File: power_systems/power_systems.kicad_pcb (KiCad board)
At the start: 2 copper layers, 75.7 x 39.9 mm, 13 parts, among them J1 Screw_Terminal_01x02, J2 Screw_Terminal_01x02, J3 Screw_Terminal_01x02, U1 LM2576HVS-5, U2 LM2576HVS-12

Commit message: power systems update and fc redesign
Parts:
- removed C1, C4: 100 uF, Capacitor_SMD:CP_Elec_4x3
- removed C2: 1000 uF, Capacitor_SMD:CP_Elec_4x3
- removed C3: C, Capacitor_SMD:CP_Elec_4x3
- removed D1: D_Schottky, Diode_SMD:D_0201_0603Metric
- removed J1, J2, J3: Screw_Terminal_01x02, TerminalBlock:TerminalBlock_MaiXu_MX126-5.0-02P_1x02_P5.00mm
- removed L2: L, Inductor_SMD:L_7.3x7.3_H3.5
- removed U2: LM2576HVS-12, Package_TO_SOT_SMD:TO-263-5_TabPin3
- added Q1: BSC520N15NS3GATMA1, avi_lib:TRANS_BSC520N15NS3GATMA1, F.Cu at (140.5, 69.3)
- added Q2: BSC520N15NS3GATMA1, avi_lib:TRANS_BSC520N15NS3GATMA1, F.Cu at (117.9, 84.7)
- added Q3: BSC520N15NS3GATMA1, avi_lib:TRANS_BSC520N15NS3GATMA1, F.Cu at (117.9, 91.4)
- D2: value D_Schottky -> PNE20010ER-Q; footprint Diode_SMD:D_0201_0603Metric -> avi_lib:CR_CFP3_SOD123W_NEX
- L1: value 100 uH -> 33uH; footprint Inductor_SMD:L_7.3x7.3_H3.5 -> avi_lib:7443633300
- U1: value LM2576HVS-5 -> LTC7801EFE-PBF; footprint Package_TO_SOT_SMD:TO-263-5_TabPin3 -> avi_lib:FE_24_ADI
- moved U1 86.4 mm to (140.3, 58.5)
- moved L1 58.6 mm to (123.9, 62.1)
- moved D2 42.7 mm to (105.7, 52.0)
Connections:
- D2 pad 2: GND -> /battery_step_down/DRVCC
- L1 pad 1: Net-(D1-K) -> /battery_step_down/SW
- L1 pad 2: Net-(J2-Pin_1) -> /battery_step_down/SENSE+
- U1 pad 1: Net-(J1-Pin_2) -> /battery_step_down/SENSE-
- U1 pad 2: Net-(D1-K) -> Net-(U1-SS)
- U1 pad 3: GND -> Net-(U1-VFB)
- U1 pad 4: Net-(J2-Pin_1) -> Net-(U1-ITH)
- U1 pad 5: GND -> Net-(U1-CRUMPEN)
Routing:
- net Net-(J3-Pin_1): track 56.9 -> 0.00 mm
- net Net-(J1-Pin_2): track 55.2 -> 0.00 mm
- net Net-(J2-Pin_1): track 55.0 -> 0.00 mm
- net Net-(D1-K): track 49.4 -> 0.00 mm
- net Net-(D2-K): track 45.5 -> 0.00 mm
- net GND: vias 3 -> 0
- removed copper zone on B.Cu, net GND
- removed copper zone on F.Cu, net GND
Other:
- board outline removed
- board text removed: "+12V"
- board text removed: "+5V"
- board text removed: "+V"
- board text removed: "GND"

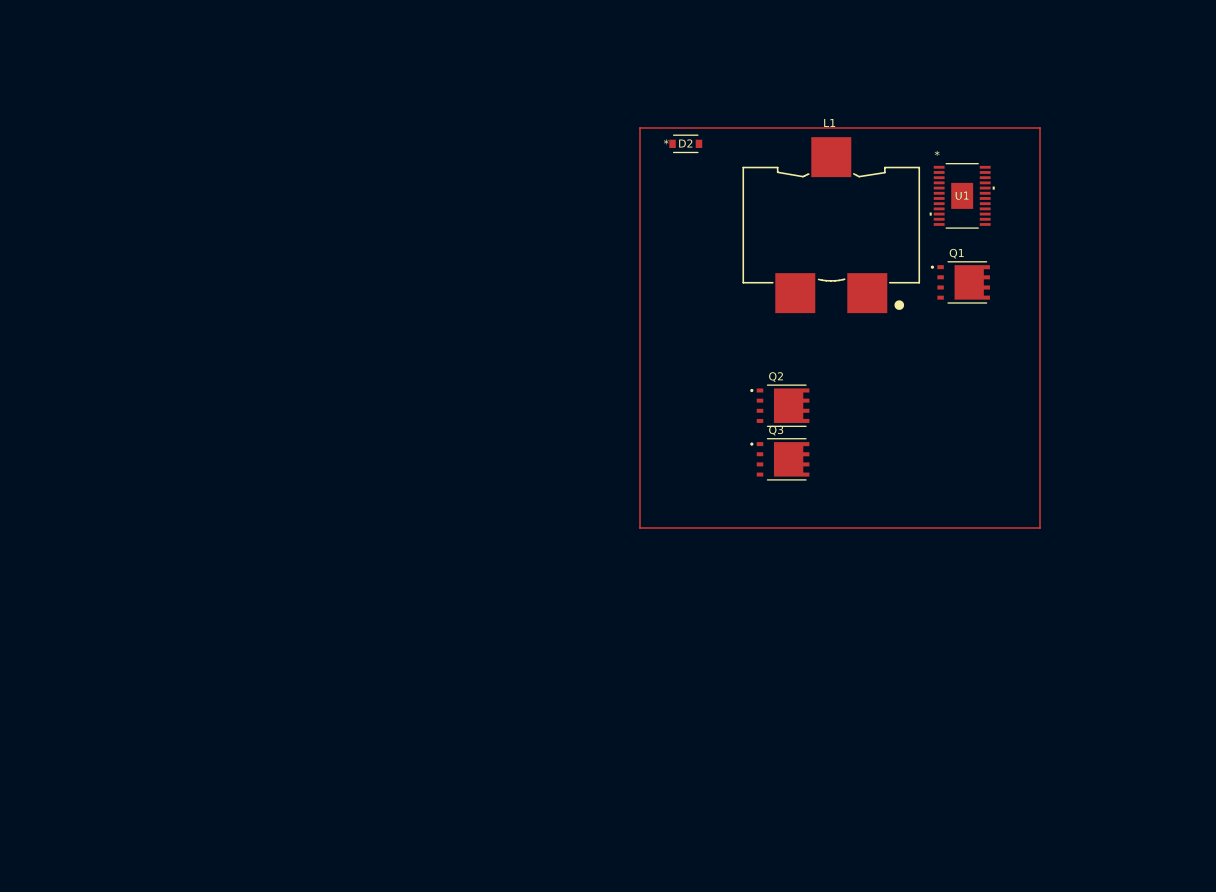
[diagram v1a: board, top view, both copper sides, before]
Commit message: Schematics and layouting for power systems board
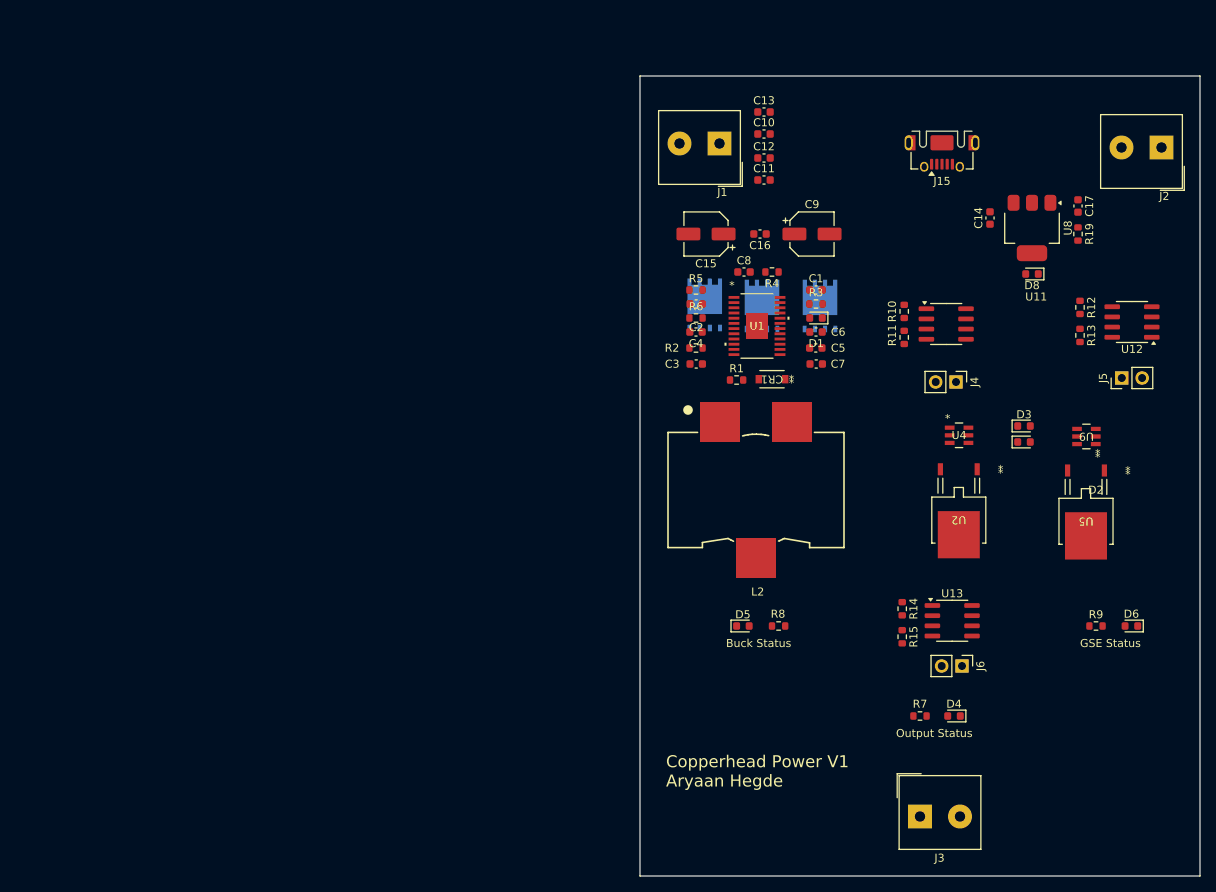
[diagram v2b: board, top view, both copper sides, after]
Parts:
- removed L1: 33uH, avi_lib:7443633300
- removed Q1, Q2: BSC520N15NS3GATMA1, avi_lib:TRANS_BSC520N15NS3GATMA1
- added C1: 0.1uF, Capacitor_SMD:C_0603_1608Metric, F.Cu at (122.0, 70.2)
- added C10: 0.47uF, Capacitor_SMD:C_0603_1608Metric, F.Cu at (115.5, 50.8)
- added C11: 0.47uF, Capacitor_SMD:C_0603_1608Metric, F.Cu at (115.5, 56.5)
- added C12: 0.47uF, Capacitor_SMD:C_0603_1608Metric, F.Cu at (115.5, 53.8)
- added C13: 0.47uF, Capacitor_SMD:C_0603_1608Metric, F.Cu at (115.5, 48.0)
- added C14: 22uF, Capacitor_SMD:C_0603_1608Metric, F.Cu at (143.8, 61.2)
- added C15: 68uF, Capacitor_SMD:CP_Elec_5x3, F.Cu at (108.2, 63.2)
- added C16: 10uF, Capacitor_SMD:C_0603_1608Metric, F.Cu at (115.0, 63.2)
- added C17: 22uF, Capacitor_SMD:C_0603_1608Metric, F.Cu at (154.8, 59.8)
- added C2: 0.1uF, Capacitor_SMD:C_0603_1608Metric, F.Cu at (107.0, 72.0)
- added C3: 100pF, Capacitor_SMD:C_0603_1608Metric, F.Cu at (107.0, 79.5)
- added C4: 3.3nF, Capacitor_SMD:C_0603_1608Metric, F.Cu at (107.0, 75.5)
- added C5: 4.7uF, Capacitor_SMD:C_0603_1608Metric, F.Cu at (122.0, 77.5)
- added C6: 1uF, Capacitor_SMD:C_0603_1608Metric, F.Cu at (122.0, 75.5)
- added C7: 0.1uF, Capacitor_SMD:C_0603_1608Metric, F.Cu at (122.0, 79.5)
- added C8: 0.1uF, Capacitor_SMD:C_0603_1608Metric, F.Cu at (113.0, 68.0)
- added C9: 100uF, Capacitor_SMD:CP_Elec_5x3, F.Cu at (121.5, 63.2)
- added CR1: PNE20010ER-QX, footprints:CR_CFP3_SOD123W_NEX, F.Cu at (116.5, 81.4)
- added D1: DS18015, Diode_SMD:D_0603_1608Metric, F.Cu at (122.0, 73.8)
- added D3: D_Schottky, Diode_SMD:D_0603_1608Metric, F.Cu at (148.0, 87.2)
- added D4: LED_VOUT, Diode_SMD:D_0603_1608Metric, F.Cu at (139.2, 123.5)
- added D5: LED_24, Diode_SMD:D_0603_1608Metric, F.Cu at (112.9, 112.2)
- added D6: LED_GSE, Diode_SMD:D_0603_1608Metric, F.Cu at (161.4, 112.2)
- added D8: LED_STM, Diode_SMD:D_0603_1608Metric, F.Cu at (149.0, 68.2)
- added J1: Screw_Terminal_01x02, TerminalBlock_Altech:Altech_AK100_1x02_P5.00mm, F.Cu at (109.9, 51.9)
- added J15: USB_B_Micro, Connector_USB:USB_Micro-AB_Molex_47590-0001, F.Cu at (137.8, 51.5)
- added J2: Screw_Terminal_01x02, TerminalBlock_Altech:Altech_AK100_1x02_P5.00mm, F.Cu at (165.2, 52.4)
- added J3: Screw_Terminal_01x02, TerminalBlock_Altech:Altech_AK100_1x02_P5.00mm, F.Cu at (135.0, 136.1)
- added J4: Conn_01x02_Pin, Connector_PinHeader_2.54mm:PinHeader_1x02_P2.54mm_Vertical, F.Cu at (139.5, 81.8)
- added J5: Conn_01x02_Pin, Connector_PinHeader_2.54mm:PinHeader_1x02_P2.54mm_Vertical, F.Cu at (160.2, 81.2)
- added J6: Conn_01x02_Pin, Connector_PinHeader_2.54mm:PinHeader_1x02_P2.54mm_Vertical, F.Cu at (140.2, 117.2)
- added L2: WE-HCF_2013, footprints:WE-HCF_2013, F.Cu at (114.5, 95.2)
- added Q4: BSC520N15NS3GATMA1, footprints:TRANS_BSC520N15NS3GATMA1, B.Cu at (122.5, 72.2)
- added Q5: BSC520N15NS3GATMA1, footprints:TRANS_BSC520N15NS3GATMA1, B.Cu at (115.2, 72.2)
- added R1: 36.5k, Resistor_SMD:R_0603_1608Metric, F.Cu at (112.1, 81.5)
- added R10: 320k, Resistor_SMD:R_0603_1608Metric, F.Cu at (133.0, 72.9)
- added R11: 40k, Resistor_SMD:R_0603_1608Metric, F.Cu at (133.0, 76.2)
- added R12: 320k, Resistor_SMD:R_0603_1608Metric, F.Cu at (155.0, 72.4)
- added R13: 40k, Resistor_SMD:R_0603_1608Metric, F.Cu at (155.0, 75.9)
- added R14: 320k, Resistor_SMD:R_0603_1608Metric, F.Cu at (132.8, 110.1)
- added R15: 40k, Resistor_SMD:R_0603_1608Metric, F.Cu at (132.8, 113.6)
- added R19: 1k5, Resistor_SMD:R_0603_1608Metric, F.Cu at (154.8, 63.2)
- added R2: R_US, Resistor_SMD:R_0603_1608Metric, F.Cu at (107.0, 77.5)
- added R3: 10, Resistor_SMD:R_0603_1608Metric, F.Cu at (122.0, 72.0)
- added R4: 6m, Resistor_SMD:R_0603_1608Metric, F.Cu at (116.5, 68.0)
- added R5: 806k, Resistor_SMD:R_0603_1608Metric, F.Cu at (107.0, 70.2)
- added R6: 28k, Resistor_SMD:R_0603_1608Metric, F.Cu at (107.0, 73.8)
- added R7: 10k, Resistor_SMD:R_0603_1608Metric, F.Cu at (135.0, 123.5)
- added R8: 10k, Resistor_SMD:R_0603_1608Metric, F.Cu at (117.3, 112.2)
- added R9: 10k, Resistor_SMD:R_0603_1608Metric, F.Cu at (157.0, 112.2)
- added U11: OPA333xxD, Package_SO:SOIC-8_3.9x4.9mm_P1.27mm, F.Cu at (138.3, 74.5)
- added U12: OPA333xxD, Package_SO:SOIC-8_3.9x4.9mm_P1.27mm, F.Cu at (161.5, 74.2)
- added U13: OPA333xxD, Package_SO:SOIC-8_3.9x4.9mm_P1.27mm, F.Cu at (139.0, 111.6)
- added U2: TK25S06N1L_LQ, footprints:DPAK&plus__TOS, F.Cu at (139.8, 99.0)
- added U4: LM5050MK-1/NOPB, footprints:MK06A, F.Cu at (139.9, 88.4)
- added U5: TK25S06N1L_LQ, footprints:DPAK&plus__TOS, F.Cu at (155.8, 99.2)
- added U8: AMS1117-3.3, Package_TO_SOT_SMD:SOT-223-3_TabPin2, F.Cu at (149.0, 62.5)
- added U9: LM5050MK-1/NOPB, footprints:MK06A, F.Cu at (155.8, 88.6)
- D2: value PNE20010ER-Q -> D_Schottky; footprint avi_lib:CR_CFP3_SOD123W_NEX -> Diode_SMD:D_0603_1608Metric
- Q3: footprint avi_lib:TRANS_BSC520N15NS3GATMA1 -> footprints:TRANS_BSC520N15NS3GATMA1; moved to B.Cu
- U1: footprint avi_lib:FE_24_ADI -> footprints:FE_24_ADI
- moved D2 56.4 mm to (148.0, 89.2)
- moved U1 30.4 mm to (114.6, 74.8)
- moved Q3 21.6 mm to (108.1, 72.1), turned to 90 degrees
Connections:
- net /battery_step_down/VBAT renamed +BATT
- D2 pad 1: Net-(D2-K) -> +VBUCK
- D2 pad 2: /battery_step_down/DRVCC -> GND
- U1 pad 15: Net-(D2-K) -> Net-(U1-BOOST)
- U1 pad EPAD: unconnected-(U1-PadEPAD) -> GND
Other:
- board outline added: 70 x 100 mm
- board text added: "Buck Status"
- board text added: "Copperhead Power V1 Aryaan Hegde"
- board text added: "GSE Status"
- board text added: "Output Status"

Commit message: Power systems routing v1
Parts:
- removed C15: 68uF, Capacitor_SMD:CP_Elec_5x3
- removed C16: 10uF, Capacitor_SMD:C_0603_1608Metric
- removed D5: LED_24, Diode_SMD:D_0603_1608Metric
- removed D8: LED_STM, Diode_SMD:D_0603_1608Metric
- removed J15: USB_B_Micro, Connector_USB:USB_Micro-AB_Molex_47590-0001
- removed R19: 1k5, Resistor_SMD:R_0603_1608Metric
- removed R8: 10k, Resistor_SMD:R_0603_1608Metric
- removed U11, U12, U13: OPA333xxD, Package_SO:SOIC-8_3.9x4.9mm_P1.27mm
- removed U8: AMS1117-3.3, Package_TO_SOT_SMD:SOT-223-3_TabPin2
- C14: value 22uF -> 10uF
- C17: value 22uF -> 68uF; footprint Capacitor_SMD:C_0603_1608Metric -> Capacitor_SMD:CP_Elec_5x3
- Q3, Q4, Q5: moved to F.Cu
- moved C17 47.1 mm to (107.8, 63.2), turned to 180 degrees
- moved J6 36.1 mm to (133.5, 81.8), turned to 90 degrees
- moved C14 29.1 mm to (114.8, 63.2), turned to 0 degrees
- moved Q3 28.4 mm to (136.5, 72.2)
- moved R15 24.2 mm to (130.6, 89.5), turned to 0 degrees
- moved R14 22.7 mm to (130.5, 87.5), turned to 180 degrees
- moved R10 17.7 mm to (139.8, 89.2), turned to 180 degrees
- moved R12 16.7 mm to (147.3, 87.2), turned to 180 degrees
- moved Q5 15.8 mm to (130.2, 67.2)
- moved R13 15.4 mm to (147.3, 89.2), turned to 0 degrees
- moved R11 12.8 mm to (139.8, 87.0), turned to 0 degrees
- moved J5 11.0 mm to (149.3, 81.8)
- moved Q4 8.66 mm to (130.2, 76.1)
- moved D4 7.80 mm to (131.7, 121.5), turned to 0 degrees
- moved J3 7.10 mm to (131.8, 129.8)
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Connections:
- net +BATT renamed /battery_step_down/+BATT
- net +GSE renamed /input_power_terminals/+GSE
- net +VOUT renamed /output_power_terminals/+VOUT
- C14 pad 1: GND -> /battery_step_down/SENSE-
- C14 pad 2: +VBUS -> GND
- C17 pad 1: GND -> /battery_step_down/SENSE-
- C17 pad 2: +3.3V -> GND
- C8 pad 1: /battery_step_down/SENSE+ -> GND
- D2 pad 1: +VBUCK -> /battery_step_down/SENSE-
- J4 pad 1: /sense_terminals/VBUCK_SENSE -> /output_power_terminals/VBUCK_SENSE
- J5 pad 1: /sense_terminals/GSE_SENSE -> /output_power_terminals/GSE_SENSE
- J6 pad 1: /sense_terminals/VOUT_SENSE -> /output_power_terminals/VOUT_SENSE
- L2 pad 2: /battery_step_down/SENSE+ -> GND
- R10 pad 1: +VBUCK -> /battery_step_down/SENSE-
- R10 pad 2: Net-(U11-+) -> /output_power_terminals/VBUCK_SENSE
- R11 pad 1: Net-(U11-+) -> /output_power_terminals/VBUCK_SENSE
- R12 pad 2: Net-(U12-+) -> /output_power_terminals/GSE_SENSE
- R13 pad 1: Net-(U12-+) -> /output_power_terminals/GSE_SENSE
- R14 pad 2: Net-(U13-+) -> /output_power_terminals/VOUT_SENSE
- R15 pad 1: Net-(U13-+) -> /output_power_terminals/VOUT_SENSE
- R3 pad 1: +VBUCK -> /battery_step_down/SENSE-
- R4 pad 1: /battery_step_down/SENSE+ -> GND
- R5 pad 1: Net-(U1-VFB) -> GND
- R6 pad 2: Net-(U1-VFB) -> GND
- U1 pad 24: /battery_step_down/SENSE+ -> GND
- U1 pad 3: Net-(U1-VFB) -> GND
- U1 pad 9: /battery_step_down/POWER_GOOD -> unconnected-(U1-PGOOD-Pad9)
- U2 pad 3: +VBUCK -> /battery_step_down/SENSE-
- U4 pad 4: +VBUCK -> /battery_step_down/SENSE-
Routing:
- net GND: track 0.00 -> 83.9 mm, vias 0 -> 10
- net /battery_step_down/SENSE-: track 0.00 -> 23.0 mm
- net /battery_step_down/SW: track 0.00 -> 14.9 mm
- net Net-(U1-CRUMPEN): track 0.00 -> 13.1 mm
- net Net-(U1-BOOST): track 0.00 -> 12.0 mm
- net Net-(U1-ITH): track 0.00 -> 7.84 mm
- net Net-(U1-FREQ): track 0.00 -> 6.44 mm
- net /battery_step_down/DRVCC: track 0.00 -> 4.45 mm
- net Net-(U1-SS): track 0.00 -> 4.02 mm
- net Net-(C4-Pad1): track 0.00 -> 2.42 mm
- added copper zone on In1.Cu, net GND
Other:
- board size 70 x 100 mm -> 65.5 x 93 mm
- copper layers 2 -> 4
